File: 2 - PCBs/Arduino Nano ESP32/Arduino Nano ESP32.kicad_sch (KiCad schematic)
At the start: 1 part, among them J1 USB4056-03-A

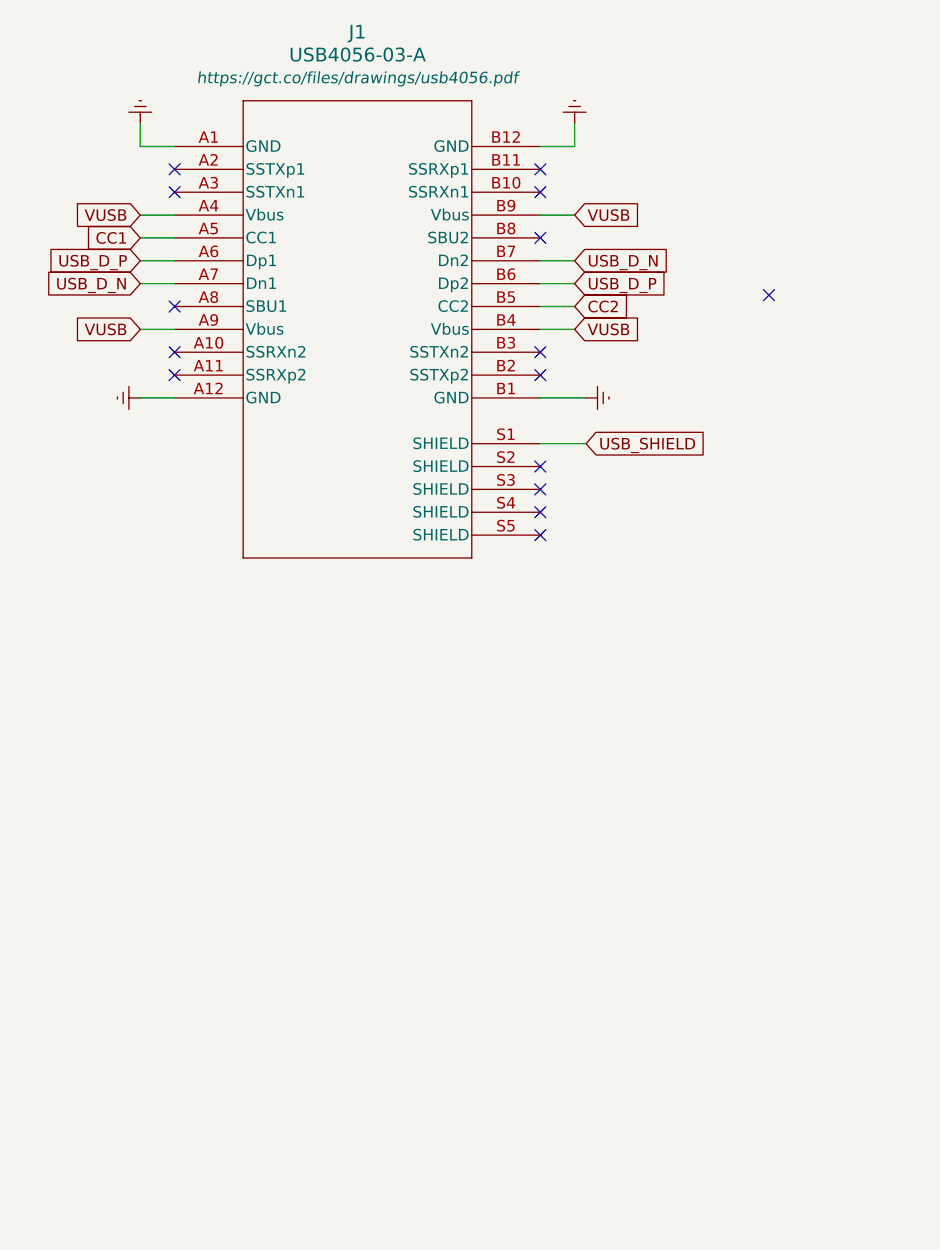
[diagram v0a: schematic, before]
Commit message: Added ESD Protection and CC Resistors
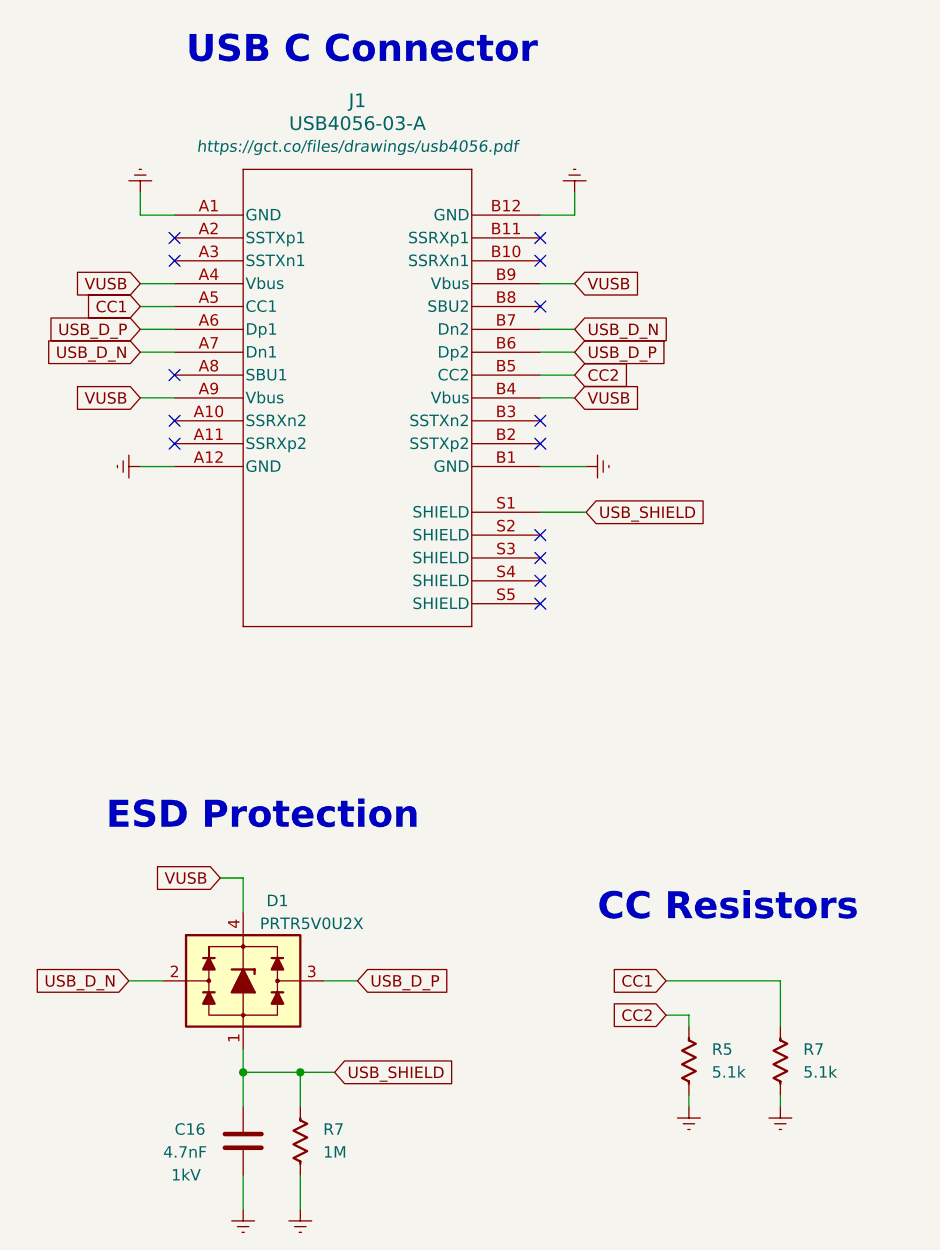
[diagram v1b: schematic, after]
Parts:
- added C16: 4.7nF, Capacitor_SMD_AKL:C_0603_1608Metric, symbol Capacitor_US_AKL:C_0603
- added D1: PRTR5V0U2X, Package_TO_SOT_SMD_AKL:SOT-143, symbol Diode_TVS_AKL:PRTR5V0U2X
- added R5, R7: 5.1k, Resistor_SMD_AKL:R_0603_1608Metric, symbol Resistor_US_AKL:R_0603
- added R7: 1M, Resistor_SMD_AKL:R_0603_1608Metric, symbol Resistor_US_AKL:R_0603
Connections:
- net CC1: now also R7.1
- net CC2: now also R5.1
- net Earth: now also C16.2, R5.2, R7.2, R7.2
- net USB_D_N: now also D1.2 (L1)
- net USB_D_P: now also D1.3 (L2)
- net USB_SHIELD: now also C16.1, D1.1 (VN), R7.1
- net VUSB: now also D1.4 (VP)
- no-connect marks 15 -> 14
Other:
- note added: "CC Resistors"
- note added: "ESD Protection"
- note added: "USB C Connector"
- moved on the sheet: J1

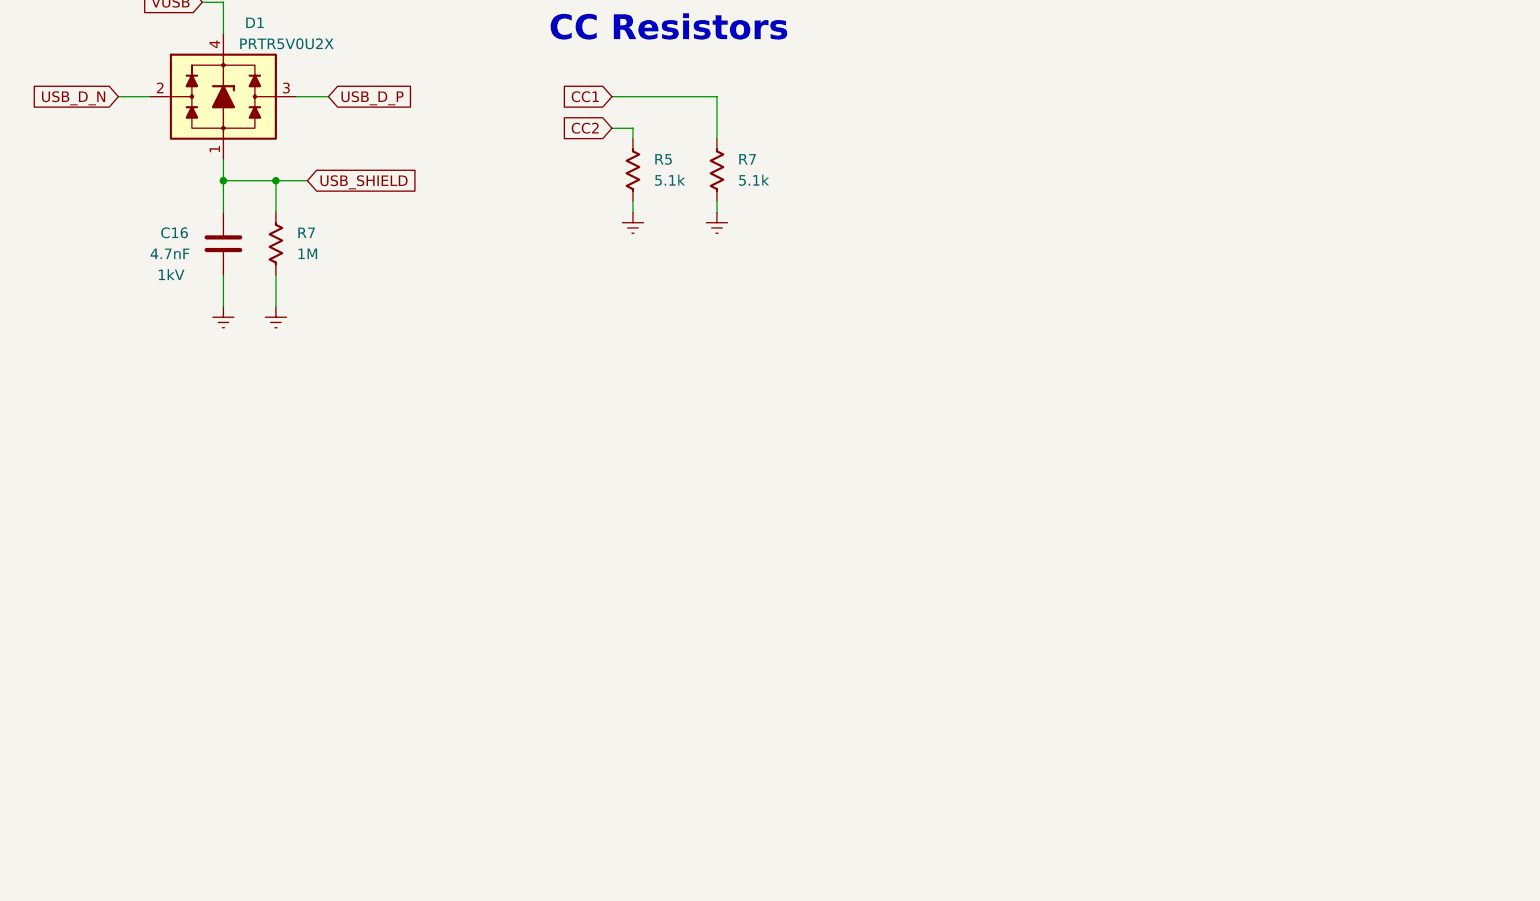
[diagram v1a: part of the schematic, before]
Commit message: Added Step Down Converter Circuit
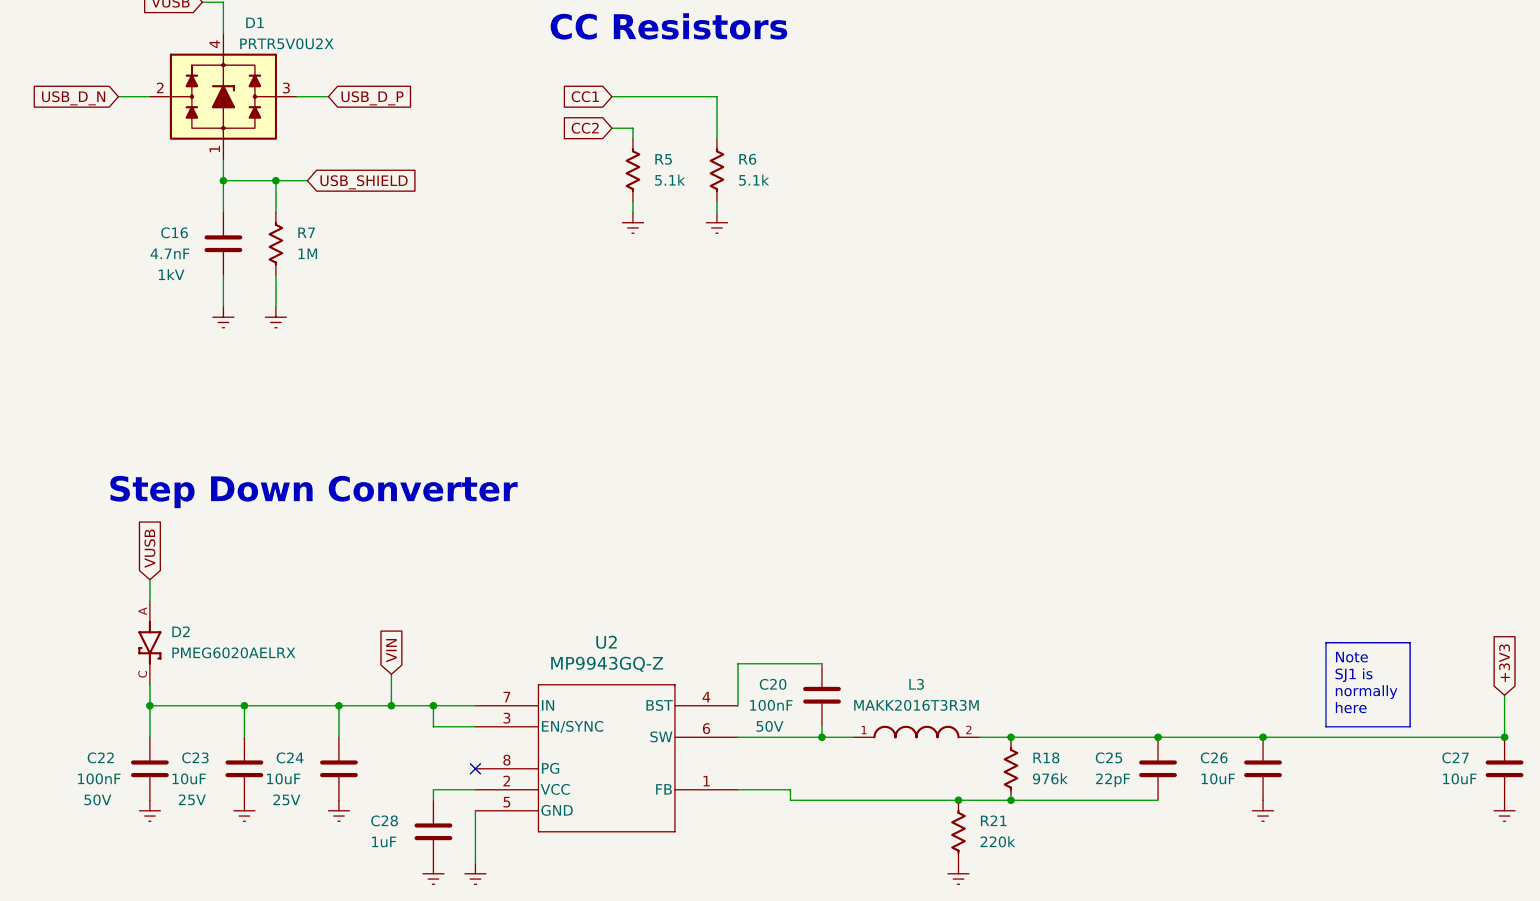
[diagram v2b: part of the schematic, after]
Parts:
- added C20, C22: 100nF, Capacitor_SMD_AKL:C_0603_1608Metric, symbol Capacitor_US_AKL:C_0603
- added C23, C24, C26, C27: 10uF, Capacitor_SMD_AKL:C_0603_1608Metric, symbol Capacitor_US_AKL:C_0603
- added C25: 22pF, Capacitor_SMD_AKL:C_0603_1608Metric, symbol Capacitor_US_AKL:C_0603
- added C28: 1uF, Capacitor_SMD_AKL:C_0603_1608Metric, symbol Capacitor_US_AKL:C_0603
- added D2: PMEG6020AELRX, PMEG6020AELRX:PMEG6020AELRX, symbol PMEG6020AELRX:PMEG6020AELRX
- added L3: MAKK2016T3R3M, MAKK2016T3R3M:MAKK2016T3R3M, symbol MAKK2016T3R3M:MAKK2016T3R3M
- added R18: 976k, Resistor_SMD_AKL:R_0603_1608Metric, symbol Resistor_US_AKL:R_0603
- added R21: 220k, Resistor_SMD_AKL:R_0603_1608Metric, symbol Resistor_US_AKL:R_0603
- added U2: MP9943GQ-Z, MP9943GQ-Z:MP9943GQ-Z, symbol MP9943GQ-Z:MP9943GQ-Z
- renumbered R7 to R6
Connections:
- net Earth: now also C22.2, C23.2, C24.2, C26.2, C27.2, C28.2, R21.2, U2.5 (GND)
- net VUSB: now also D2.A
- new net: C25.2, R18.2, R21.1, U2.1 (FB)
- new net: C20.2, L3.1, U2.6 (SW)
- new net: C20.1, U2.4 (BST)
- new net: C28.1, U2.2 (VCC)
- new net +3V3: C25.1, C26.1, C27.1, L3.2, R18.1
- new net VIN: C22.1, C23.1, C24.1, D2.C, U2.3 (EN/SYNC), U2.7 (IN)
- no-connect marks 14 -> 15
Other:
- note added: "Step Down Converter"

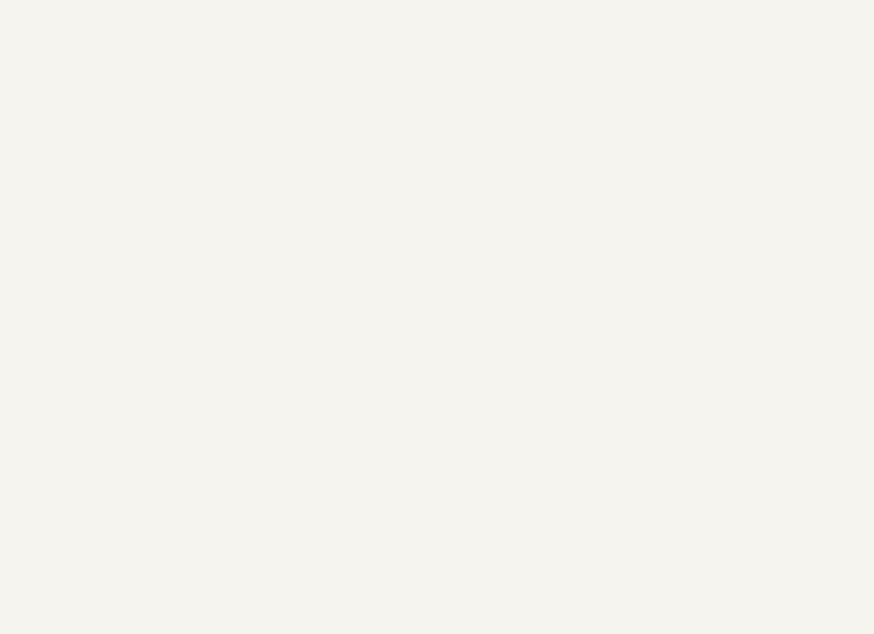
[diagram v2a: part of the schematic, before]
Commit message: Finished flash schematic
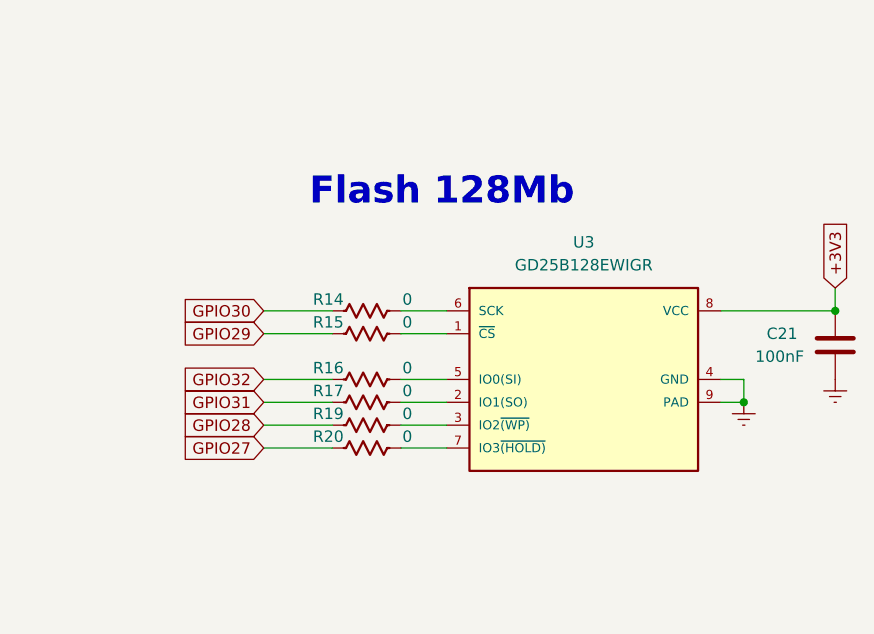
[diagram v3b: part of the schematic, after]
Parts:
- added C21: 100nF, Capacitor_SMD_AKL:C_0603_1608Metric, symbol Capacitor_US_AKL:C_0603
- added R14, R15, R16, R17, R19, R20: 0, Resistor_SMD_AKL:R_0603_1608Metric, symbol Resistor_US_AKL:R_0603
- added U3: GD25B128EWIGR, GD25B128EWIGR_128Mb:GD25B128EWIGR_128Mb, symbol GD25B128EWIGR_128Mb:GD25B128EWIGR
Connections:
- net +3V3: now also C21.1, U3.8 (VCC)
- net Earth: now also C21.2, U3.4 (GND), U3.9 (PAD)
- new net: R20.2, U3.7 (IO3~{(HOLD)})
- new net: R15.2, U3.1 (~{CS})
- new net: R17.2, U3.2 (IO1(SO))
- new net: R19.2, U3.3 (IO2~{(WP)})
- new net: R16.2, U3.5 (IO0(SI))
- new net: R14.2, U3.6 (SCK)
- new net GPIO27: R20.1
- new net GPIO28: R19.1
- new net GPIO29: R15.1
- new net GPIO30: R14.1
- new net GPIO31: R17.1
- new net GPIO32: R16.1
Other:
- note added: "Flash 128Mb"
